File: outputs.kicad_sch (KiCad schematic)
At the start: 22 parts, among them Q1 ISL9V3040D3ST, Q2 ISL9V3040D3ST, U2 VNLD5160TR-E, U3 VNLD5160TR-E, U4 VNLD5160TR-E, U5 TLE9201SGAUMA1, U6 VNLD5160TR-E

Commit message: redone layout, possibly feature complete
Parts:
- removed U5: TLE9201SGAUMA1, TLE9201SG:TLE9201SGAUMA1_INF, symbol TLE9201SG:TLE9201SGAUMA1
- added IC1: TLE9201SG, TLE9201SG:TLE9201SG, symbol TLE9201SG:TLE9201SG
- added R17, R18, R19, R20: 4.7k, Resistor_SMD:R_0402_1005Metric, symbol Device:R_Small
- added U7, U8: VNLD5160TR-E, VNLD5160TR-E:SO_160TR-E_STM, symbol VNLD5160TR-E:VNLD5160TR-E
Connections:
- net +12V: now also IC1.4 (VS)
- net +3V3: now also IC1.2 (VSO)
- net ACR_2: now also U2.6 (DRAIN2); no longer U3.6 (DRAIN2)
- net ETC_DIR: now also IC1.1 (DIR)
- net ETC_OUT_M: now also IC1.5 (OUT1)
- net ETC_OUT_P: now also IC1.7 (OUT2)
- net ETC_PWM: now also IC1.12 (PWM)
- net FIVVTC: now also U4.6 (DRAIN2); no longer U4.8 (DRAIN1)
- net GND: now also IC1.10 (SCK), IC1.13 (GNDPAD), IC1.14 (GND_2), IC1.15 (GND_3), IC1.6 (GND_1), IC1.8 (SI), IC1.9 (CSN), R17.2, R18.2, R19.2, R20.2, U7.5 (SOURCE2), U7.7 (SOURCE1), U8.5 (SOURCE2), U8.7 (SOURCE1)
- net INJ_1: now also U3.6 (DRAIN2); no longer U2.8 (DRAIN1)
- net INJ_2: now also U2.8 (DRAIN1); no longer U2.6 (DRAIN2)
- net MCU_ACR2: now also R4.1, U2.3 (IN2/VSUPPLY2); no longer R6.1, U3.3 (IN2/VSUPPLY2)
- net MCU_INJ1: now also R6.1, U3.3 (IN2/VSUPPLY2); no longer R3.1, U2.1 (IN1/VSUPPLY1)
- net MCU_INJ2: now also R3.1, U2.1 (IN1/VSUPPLY1); no longer R4.1, U2.3 (IN2/VSUPPLY2)
- net PRGSEL: now also U4.8 (DRAIN1); no longer U4.6 (DRAIN2)
- net at R14.1: now also IC1.11 (DIS)
- new net CCFC: U8.8 (DRAIN1)
- new net FHO2H: U8.6 (DRAIN2)
- new net MCU_CCFC: R19.1, U8.1 (IN1/VSUPPLY1)
- new net MCU_FHO2H: R20.1, U8.3 (IN2/VSUPPLY2)
- new net MCU_PCHO2SHTR: R18.1, U7.3 (IN2/VSUPPLY2)
- new net MCU_RHO2H: R17.1, U7.1 (IN1/VSUPPLY1)
- new net PCHO2SHTR: U7.6 (DRAIN2)
- new net RHO2H: U7.8 (DRAIN1)
- no-connect marks 9 -> 13
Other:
- note added: "CCFC & HO2HTR"
- note added: "H2OS Heaters"
- note added: "INJECTORS & ACR"
- note added: "INJECTORS MEASURED TO TAKE AROUND 1A EACH"
- note removed: "ACR"
- note removed: "INJECTORS"
- moved on the sheet: Q1, Q2, R11, R12, R13, R15, R16, R3, R4, R5, R6, R8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

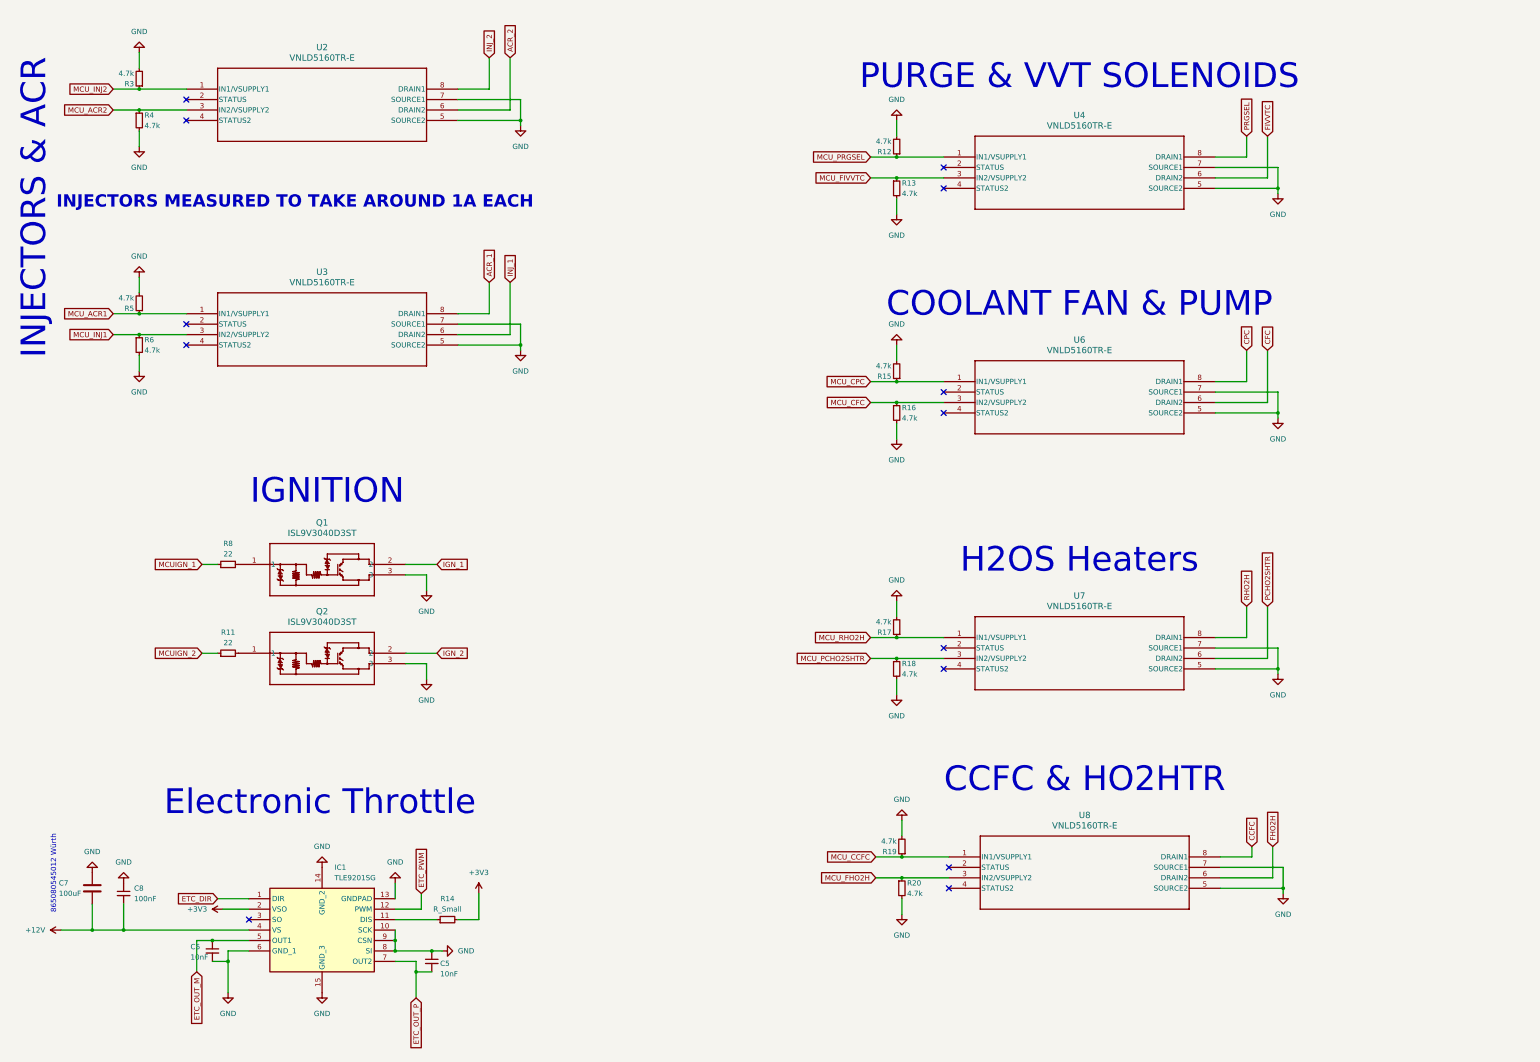
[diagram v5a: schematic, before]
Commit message: Proper stronger mosfet for coolant fan and pump
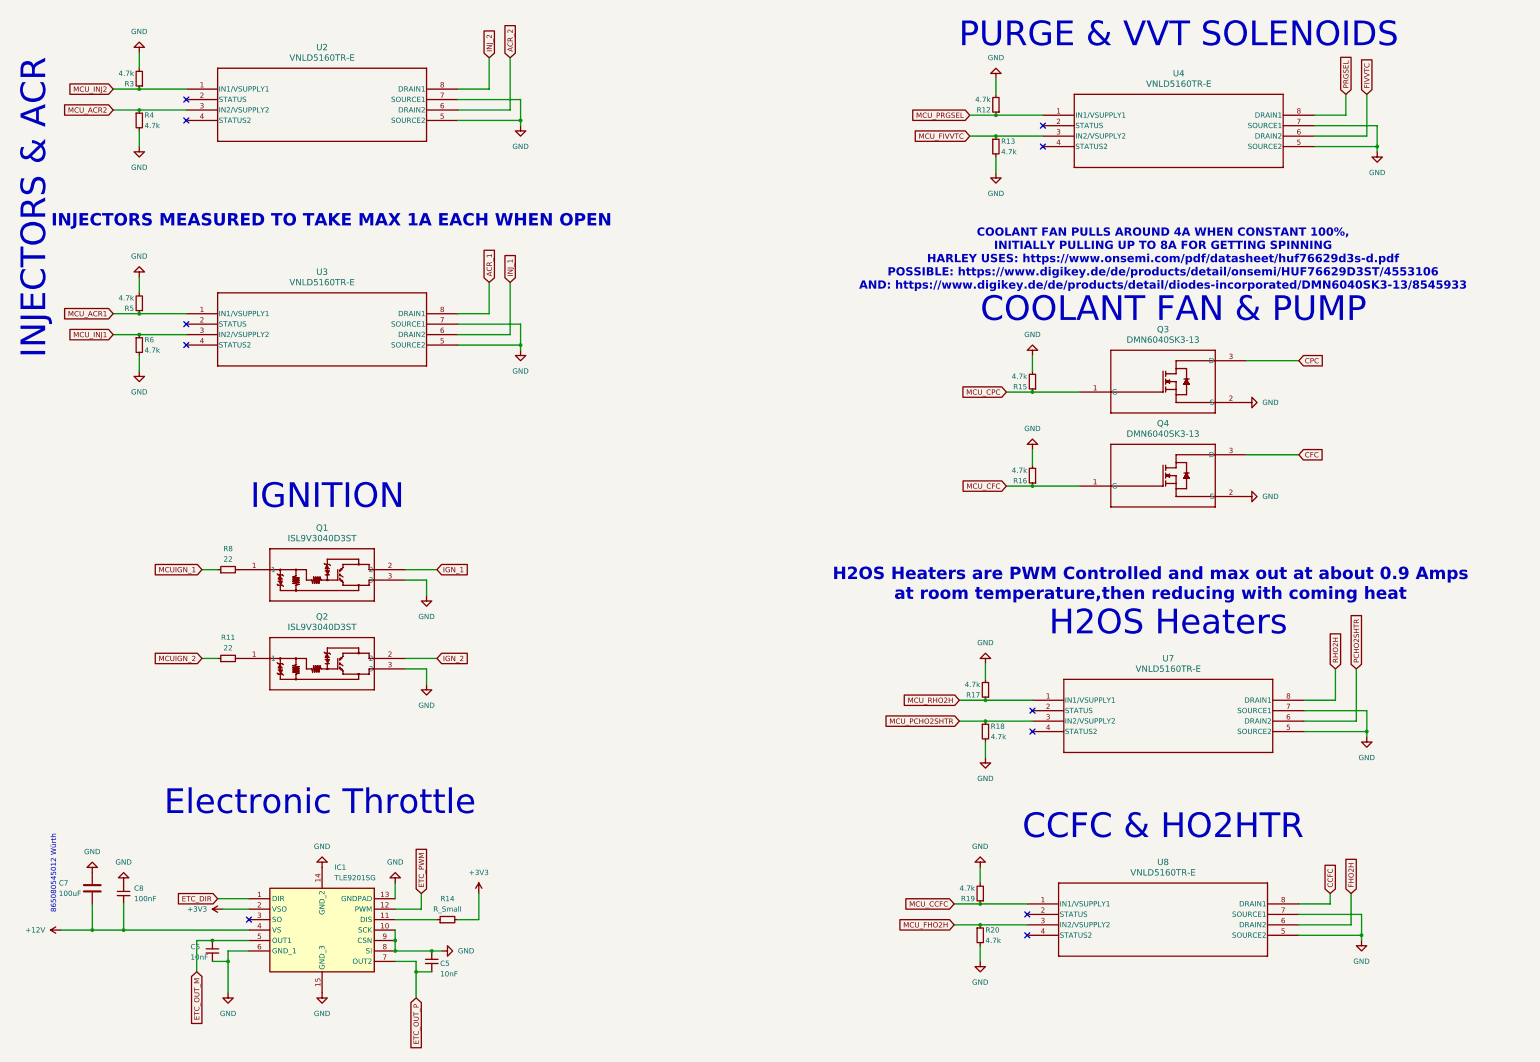
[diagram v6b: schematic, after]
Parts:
- removed U6: VNLD5160TR-E, VNLD5160TR-E:SO_160TR-E_STM, symbol VNLD5160TR-E:VNLD5160TR-E
- added Q3, Q4: DMN6040SK3-13, DMN6040SK3_13:D-PAK_DMN6040SK3-13_DIO, symbol DMN6040SK3_13:DMN6040SK3-13
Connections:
- net CFC: now also Q4.3 (D)
- net CPC: now also Q3.3 (D)
- net GND: now also Q3.2 (S), Q4.2 (S)
- net MCU_CFC: now also Q4.1 (G)
- net MCU_CPC: now also Q3.1 (G)
- no-connect marks 13 -> 11
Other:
- note added: "COOLANT FAN PULLS AROUND 4A WHEN CONSTANT 100%, INITIALLY PULLING UP TO 8A FOR GETTING SPINNING HARLEY USES: https://www.onsemi.com/pdf/datasheet/huf76629d3s-d.pdf POSSIBLE: https://www.digikey.de/de/products/detail/onsemi/HUF76629D3ST/4553106 AND: https://www.digikey.de/de/products/detail/diodes-incorporated/DMN6040SK3-13/8545933"
- note added: "H2OS Heaters are PWM Controlled and max out at about 0.9 Amps at room temperature,then reducing with coming heat"
- note added: "INJECTORS MEASURED TO TAKE MAX 1A EACH WHEN OPEN"
- note removed: "INJECTORS MEASURED TO TAKE AROUND 1A EACH"
- moved on the sheet: Q1, Q2, R11, R12, R13, R15, R16, R17, R18, R19, R20, R8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

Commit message: pwm for heaters, minor routing and via changes, teardrops
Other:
- note added: "COOLANT FAN PULLS AROUND 4A WHEN CONSTANT 100%, INITIALLY PULLING UP TO 8A FOR GETTING SPINNING HARLEY USES: HUFA76429D3 POSSIBLE: https://www.digikey.de/de/products/detail/onsemi/HUF76629D3ST/4553106 AND: https://www.digikey.de/de/products/detail/diodes-incorporated/DMN6040SK3-13/8545933"
- note added: "H2OS Heaters are PWM Controlled and max out at about 0.9 Amps at room temperature, then reducing with coming heat"
- note added: "Harley Uses: https://www.mouser.de/ProductDetail/onsemi/FGB3040G2-F085C?qs=2WXlatMagcHzMRj1hscbYQ%3D%3D"
- note removed: "COOLANT FAN PULLS AROUND 4A WHEN CONSTANT 100%, INITIALLY PULLING UP TO 8A FOR GETTING SPINNING HARLEY USES: https://www.onsemi.com/pdf/datasheet/huf76629d3s-d.pdf POSSIBLE: https://www.digikey.de/de/products/detail/onsemi/HUF76629D3ST/4553106 AND: https://www.digikey.de/de/products/detail/diodes-incorporated/DMN6040SK3-13/8545933"
- note removed: "H2OS Heaters are PWM Controlled and max out at about 0.9 Amps at room temperature,then reducing with coming heat"
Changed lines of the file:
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@@
 		)
 	)
-	(text "COOLANT FAN PULLS AROUND 4A WHEN CONSTANT 100%,\nINITIALLY PULLING UP TO 8A FOR GETTING SPINNING\nHARLEY USES: https://www.onsemi.com/pdf/datasheet/huf76629d3s-d.pdf\nPOSSIBLE: https://www.digikey.de/de/products/detail/onsemi/HUF76629D3ST/4553106\nAND: https://www.digikey.de/de/products/detail/diodes-incorporated/DMN6040SK3-13/8545933"
+	(text "COOLANT FAN PULLS AROUND 4A WHEN CONSTANT 100%,\nINITIALLY PULLING UP TO 8A FOR GETTING SPINNING\nHARLEY USES: HUFA76429D3\nPOSSIBLE: https://www.digikey.de/de/products/detail/onsemi/HUF76629D3ST/4553106\nAND: https://www.digikey.de/de/products/detail/diodes-incorporated/DMN6040SK3-13/8545933"
 		(exclude_from_sim no)
 		(at 307.34 79.502 0)
@@
 		)
 	)
-	(text "H2OS Heaters are PWM Controlled and max out at about 0.9 Amps\nat room temperature,then reducing with coming heat"
+	(text "H2OS Heaters are PWM Controlled and max out at about 0.9 Amps\nat room temperature, then reducing with coming heat"
 		(exclude_from_sim no)
 		(at 304.292 158.496 0)
@@
 			)
 		)
+	)
+	(text "Harley Uses:\nhttps://www.mouser.de/ProductDetail/onsemi/FGB3040G2-F085C?qs=2WXlatMagcHzMRj1hscbYQ%3D%3D"
+		(exclude_from_sim no)
+		(at 103.124 130.302 0)
+		(effects
+			(font
+				(size 2 2)
+				(thickness 0.4)
+				(bold yes)
+				(color 2 92 76 1)
+			)
+		)

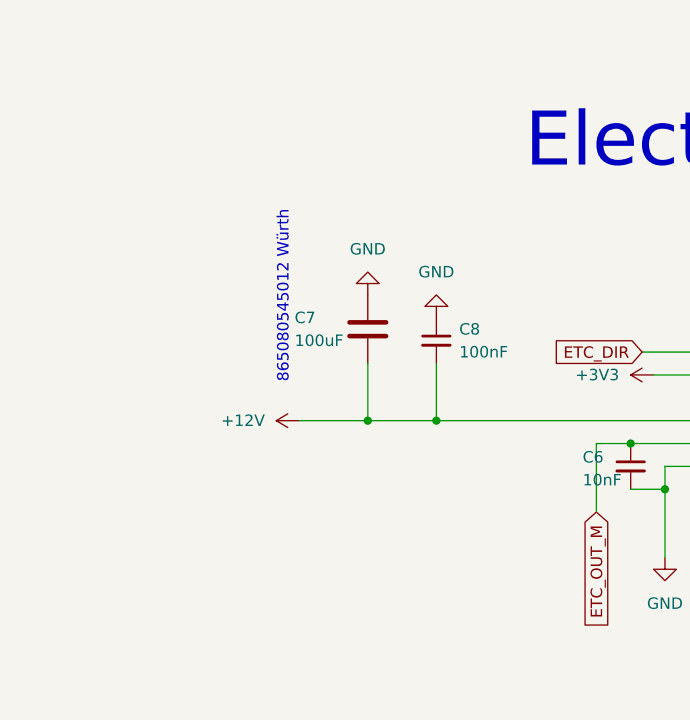
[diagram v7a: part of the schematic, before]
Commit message: large cap, more silkscreen for big connector
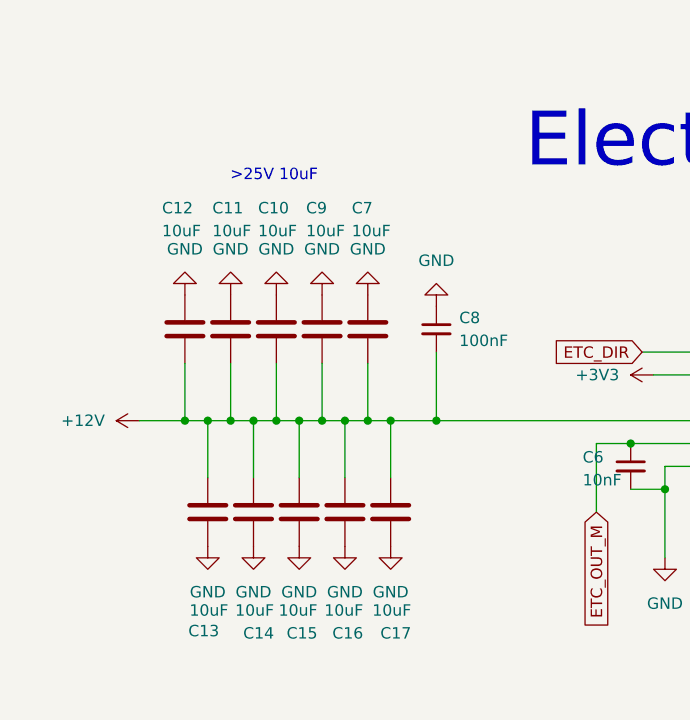
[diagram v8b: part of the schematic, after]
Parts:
- added C10, C11, C12, C13, C14, C15, C16, C17, C9: 10uF, Capacitor_SMD:C_0805_2012Metric, symbol Device:C
- C7: value 100uF -> 10uF; footprint Capacitor_SMD:C_Elec_6.3x5.8 -> Capacitor_SMD:C_0805_2012Metric
- R14: footprint (none) -> Resistor_SMD:R_0402_1005Metric
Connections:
- net +12V: now also C10.2, C11.2, C12.2, C13.2, C14.2, C15.2, C16.2, C17.2, C9.2
- net GND: now also C10.1, C11.1, C12.1, C13.1, C14.1, C15.1, C16.1, C17.1, C9.1
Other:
- note added: ">25V 10uF"
- note removed: "865080545012 Würth"
- moved on the sheet: C8
